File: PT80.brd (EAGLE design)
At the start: 75.9 x 55.9 mm, 78 parts, among them IC1 MAX1044, IC2 TL072P, IC3 78L05Z, IC4 78L12Z, Q1 2N5089

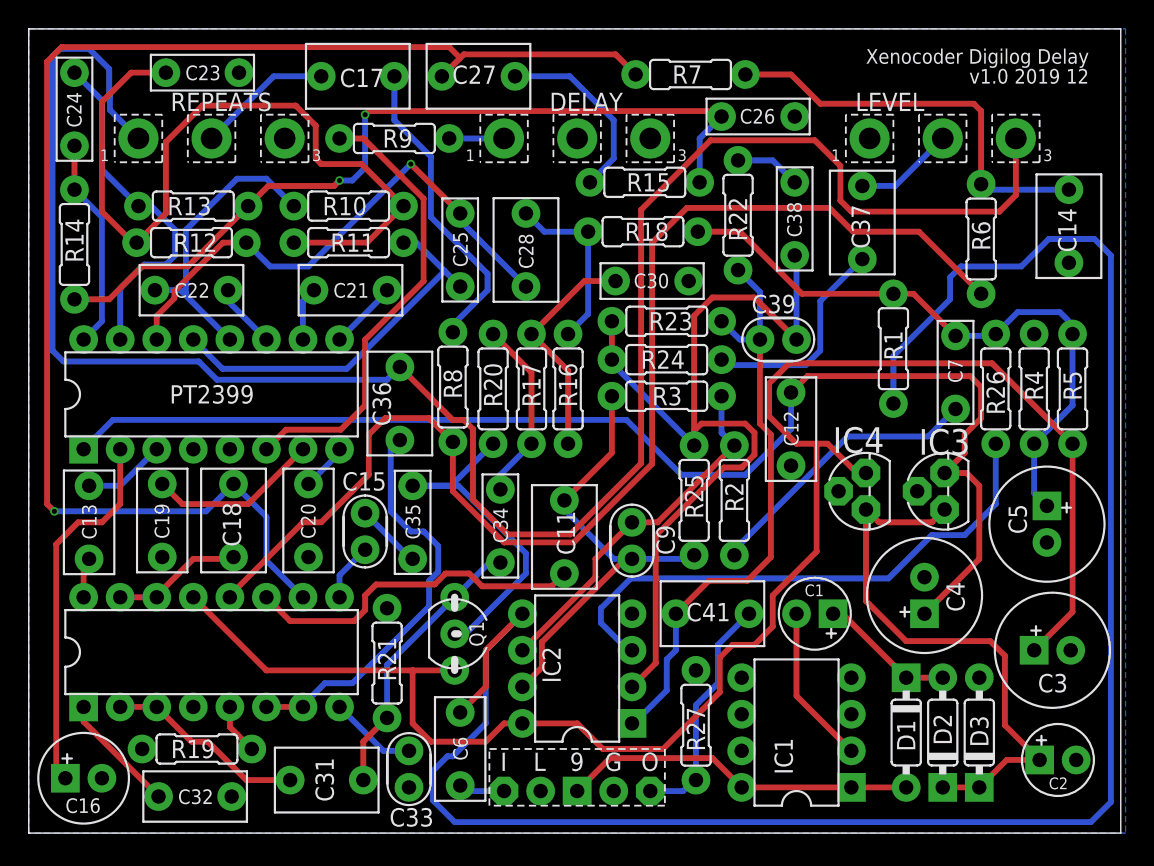
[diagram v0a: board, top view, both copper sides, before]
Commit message: Version 1.1 - Fixed repeats direction and orientation of power regulators
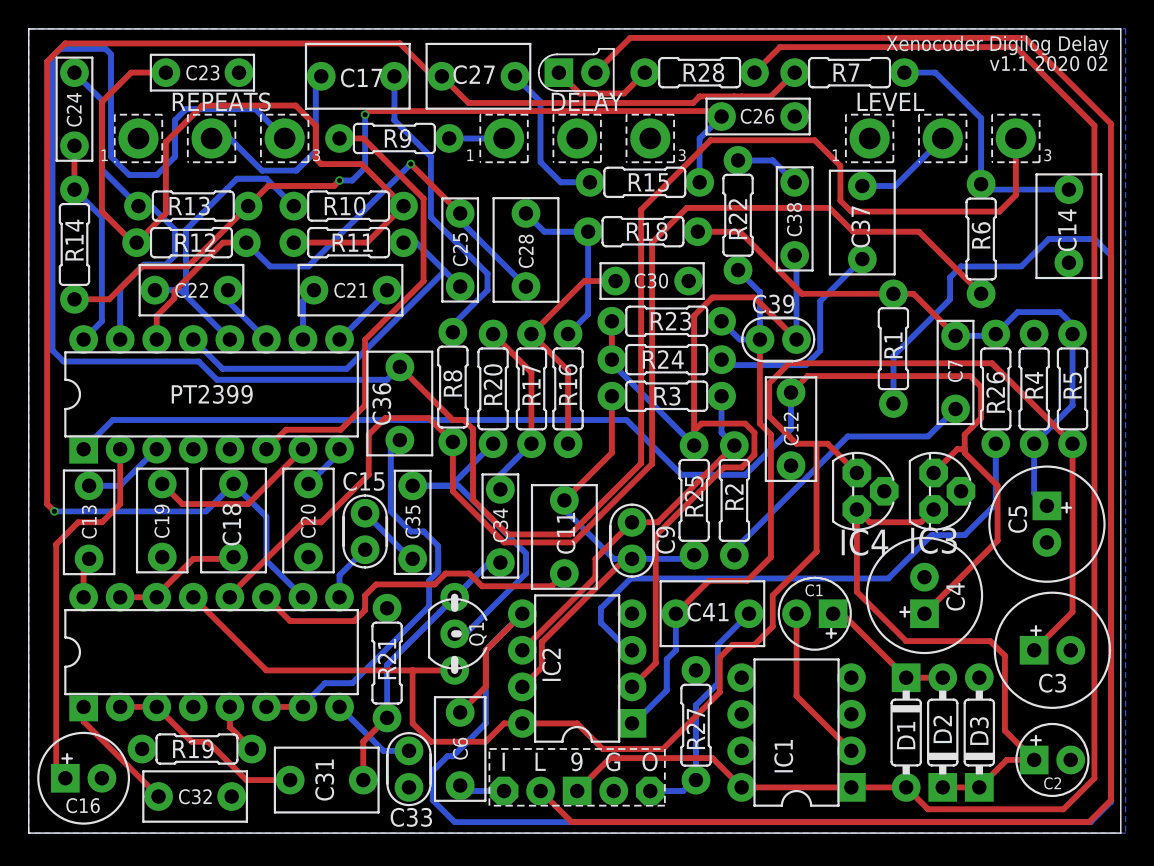
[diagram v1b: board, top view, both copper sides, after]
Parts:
- added 3MM: LED3MM, mb_diodes:LED3MM
- added R28: 4k7, mb_resistors:R0207/3
- moved R7 11.0 mm to (57.0, 52.8)
- moved IC3 0.76 mm to (62.9, 23.7), turned to 270 degrees
- moved IC4 0.63 mm to (57.5, 23.7), turned to 270 degrees
- moved C2 0.38 mm to (71.1, 5.08)
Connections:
- new net N$1: C2.+, D2.C, D3.C, IC3.3, IC4.3
- net +9V: now also R28.2
- net B: now also IC4.1; no longer IC4.3
- net D: now also 3MM.K
- net GND: now also REPEATS.1; no longer REPEATS.3
- net N$4: now also 3MM.A, R28.1; no longer C2.+, D2.C, D3.C, IC3.1, IC4.1
- net N$48: now also REPEATS.3; no longer REPEATS.1
- net N$6: now also IC3.1; no longer IC3.3
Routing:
- net D: track 0.00 -> 127.4 mm
- net +9V: track 24.6 -> 111.2 mm
- net N$1: track 0.00 -> 39.1 mm
- net N$4: track 39.5 -> 7.17 mm
- net N$48: track 136.2 -> 154.2 mm
- net N$13: track 28.8 -> 17.5 mm
- net N$15: track 98.7 -> 109.6 mm
- net N$52: track 9.41 -> 14.1 mm
- net N$32: track 13.1 -> 10.7 mm
- net N$6: track 89.7 -> 91.5 mm
- net B: track 119.7 -> 119.1 mm
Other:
- board text added: "Xenocoder Digilog Delay v1.1 2020 02"
- board text removed: "Xenocoder Digilog Delay v1.0 2019 12"
